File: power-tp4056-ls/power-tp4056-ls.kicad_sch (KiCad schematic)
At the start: 21 parts, among them J0 USB_C_Receptacle_PowerOnly_6P, J1 Conn_01x01, J2 Conn_01x01, J3 Conn_01x01, J4 Conn_01x01, J5 Conn_01x01, J6 Conn_01x01, Q1 AO3401A, U1 TP4056, U2 XB5307H

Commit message: Add LCSC part numbers for basic components
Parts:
- C1, C2: LCSC (none) -> C15850
- C3: LCSC (none) -> C28233
- D3: LCSC (none) -> C8678
- Q1: LCSC (none) -> C15127
- R1: LCSC (none) -> C17379
- R2: LCSC (none) -> C17408
- RN1: JLCPCB_CORRECTION (none) -> 0; 0; 90; LCSC (none) -> C29718
- U1: LCSC (none) -> C16581; LCSC Part C16581 -> (none)
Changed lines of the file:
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@@
 			)
 		)
+		(property "LCSC" "C29718"
+			(at 114.3 46.99 0)
+			(effects
+				(font
+					(size 1.27 1.27)
+				)
+				(hide yes)
+			)
+		)
+		(property "JLCPCB_CORRECTION" "0; 0; 90"
+			(at 114.3 46.99 90)
+			(effects
+				(font
+					(size 1.27 1.27)
+				)
+				(hide yes)
+			)
+		)
 		(pin "7"
 		)
@@
 			)
 		)
+		(property "LCSC" "C8678"
+			(at 236.22 35.56 0)
+			(effects
+				(font
+					(size 1.27 1.27)
+				)
+				(hide yes)
+			)
+		)
 		(pin "1"
 		)
@@
 			)
 		)
+		(property "LCSC" "C28233"
+			(at 252.73 71.12 0)
+			(effects
+				(font
+					(size 1.27 1.27)
+				)
+				(hide yes)
+			)
+		)
 		(pin "1"
 		)
@@
 			)
 		)
+		(property "LCSC" "C29718"
+			(at 247.65 41.91 0)
+			(effects
+				(font
+					(size 1.27 1.27)
+				)
+				(hide yes)
+			)
+		)
+		(property "JLCPCB_CORRECTION" "0; 0; 90"
+			(at 247.65 41.91 90)
+			(effects
+				(font
+					(size 1.27 1.27)
+				)
+				(hide yes)
+			)
+		)
 		(pin "7"
 		)
@@
 			)
 		)
+		(property "LCSC" "C15127"
+			(at 228.6 31.75 0)
+			(effects
+				(font
+					(size 1.27 1.27)
+				)
+				(hide yes)
+			)
+		)
 		(pin "1"
 		)
@@
 			)
 		)
+		(property "LCSC" "C17379"
+			(at 162.56 63.5 0)
+			(effects
+				(font
+					(size 1.27 1.27)
+				)
+				(hide yes)
+			)
+		)
 		(pin "1"
 		)
@@
 			)
 		)
+		(property "LCSC" "C15850"
+			(at 99.06 40.64 0)
+			(effects
+				(font
+					(size 1.27 1.27)
+				)
+				(hide yes)
+			)
+		)
 		(pin "1"
 		)
@@
 			)
 		)
+		(property "LCSC" "C17408"
+			(at 260.35 66.04 0)
+			(effects
+				(font
+					(size 1.27 1.27)
+				)
+				(hide yes)
+			)
+		)
 		(pin "2"
 		)
@@
 			)
 		)
-		(property "LCSC Part" "C16581"
-			(at 146.05 80.01 0)
+		(property "LCSC" "C16581"
+			(at 146.05 46.99 0)
 			(effects
 				(font
@@
 			)
 		)
+		(property "LCSC" "C29718"
+			(at 114.3 76.2 0)
+			(effects
+				(font
+					(size 1.27 1.27)
+				)
+				(hide yes)
+			)
+		)
+		(property "JLCPCB_CORRECTION" "0; 0; 90"
+			(at 114.3 76.2 90)
+			(effects
+				(font
+					(size 1.27 1.27)
+				)
+				(hide yes)
+			)
+		)
 		(pin "7"
 		)
@@
 			)
 		)
+		(property "LCSC" "C15850"
+			(at 179.07 36.83 0)
+			(effects
+				(font
+					(size 1.27 1.27)
+				)
+				(hide yes)
+			)
+		)
 		(pin "1"
 		)
@@
 			(effects
 				(font
+					(size 1.27 1.27)
+				)
+				(hide yes)
+			)
+		)
+		(property "LCSC" "C29718"
+			(at 114.3 59.69 0)
+			(effects
+				(font
+					(size 1.27 1.27)
+				)
+				(hide yes)
+			)
+		)
+		(property "JLCPCB_CORRECTION" "0; 0; 90"
+			(at 114.3 59.69 90)
+			(effects
+				(font

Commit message: Update LCSC part numbers and JLCPCB positioning info
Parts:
- C1, C2: LCSC C15850 -> (none); LCSC Part (none) -> C15850
- C3: LCSC C28233 -> (none); LCSC Part (none) -> C28233
- D3: LCSC C8678 -> (none); LCSC Part (none) -> C8678
- Q1: JLCPCB_CORRECTION (none) -> 0; 0; 180; LCSC C15127 -> (none); LCSC Part (none) -> C15127
- R1: LCSC C17379 -> (none); LCSC Part (none) -> C17379
- R2: LCSC C17408 -> (none); LCSC Part (none) -> C17408
- RN1: LCSC C29718 -> (none); LCSC Part (none) -> C29718
- U1: JLCPCB_CORRECTION (none) -> 0; 0; 270; LCSC C16581 -> (none); LCSC Part (none) -> C16581
- U2: JLCPCB_CORRECTION (none) -> 0; 0; 270
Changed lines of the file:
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@@
 			)
 		)
-		(property "LCSC" "C29718"
+		(property "LCSC Part" "C29718"
 			(at 114.3 46.99 0)
 			(effects
@@
 			)
 		)
-		(property "LCSC" "C8678"
+		(property "LCSC Part" "C8678"
 			(at 236.22 35.56 0)
 			(effects
@@
 			)
 		)
-		(property "LCSC" "C28233"
+		(property "LCSC Part" "C28233"
 			(at 252.73 71.12 0)
 			(effects
@@
 			)
 		)
-		(property "LCSC" "C29718"
+		(property "LCSC Part" "C29718"
 			(at 247.65 41.91 0)
 			(effects
@@
 			)
 		)
+		(property "JLCPCB_CORRECTION" "0; 0; 270"
+			(at 217.17 69.85 0)
+			(effects
+				(font
+					(size 1.27 1.27)
+				)
+				(hide yes)
+			)
+		)
 		(property "LCSC Part" "C154942"
 			(at 217.17 85.09 0)
@@
 			)
 		)
-		(property "LCSC" "C15127"
+		(property "LCSC Part" "C15127"
 			(at 228.6 31.75 0)
 			(effects
@@
 			)
 		)
+		(property "JLCPCB_CORRECTION" "0; 0; 180"
+			(at 228.6 31.75 90)
+			(effects
+				(font
+					(size 1.27 1.27)
+				)
+				(hide yes)
+			)
+		)
 		(pin "1"
 		)
@@
 			)
 		)
-		(property "LCSC" "C17379"
+		(property "LCSC Part" "C17379"
 			(at 162.56 63.5 0)
 			(effects
@@
 			)
 		)
-		(property "LCSC" "C15850"
+		(property "LCSC Part" "C15850"
 			(at 99.06 40.64 0)
 			(effects
@@
 			)
 		)
-		(property "LCSC" "C17408"
+		(property "LCSC Part" "C17408"
 			(at 260.35 66.04 0)
 			(effects
@@
 			)
 		)
-		(property "LCSC" "C16581"
+		(property "JLCPCB_CORRECTION" "0; 0; 270"
 			(at 146.05 46.99 0)
 			(effects
@@
 			)
 		)
+		(property "LCSC Part" "C16581"
+			(at 146.05 80.01 0)
+			(effects
+				(font
+					(size 1.27 1.27)
+				)
+				(hide yes)
+			)
+		)
 		(pin "9"
 		)
@@
 			)
 		)
-		(property "LCSC" "C29718"
+		(property "LCSC Part" "C29718"
 			(at 114.3 76.2 0)
 			(effects
@@
 			)
 		)
-		(property "LCSC" "C15850"
+		(property "LCSC Part" "C15850"
 			(at 179.07 36.83 0)
 			(effects
@@
 			)
 		)
-		(property "LCSC" "C29718"
+		(property "LCSC Part" "C29718"
 			(at 114.3 59.69 0)
 			(effects

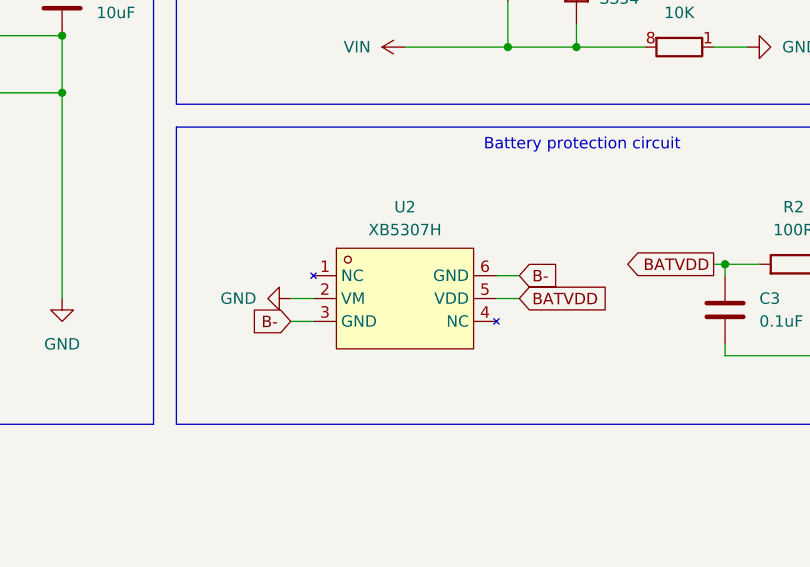
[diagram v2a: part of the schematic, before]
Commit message: Replace XB5307H with XB5350D0 for Li-Ion battery protection
XB5307H has an overcharge cutoff voltage of 4.425V, while XB5350D0 has
an overcharge cutoff voltage of 4.25V. Both ICs have an underdischarge
cutoff voltage of 3V.
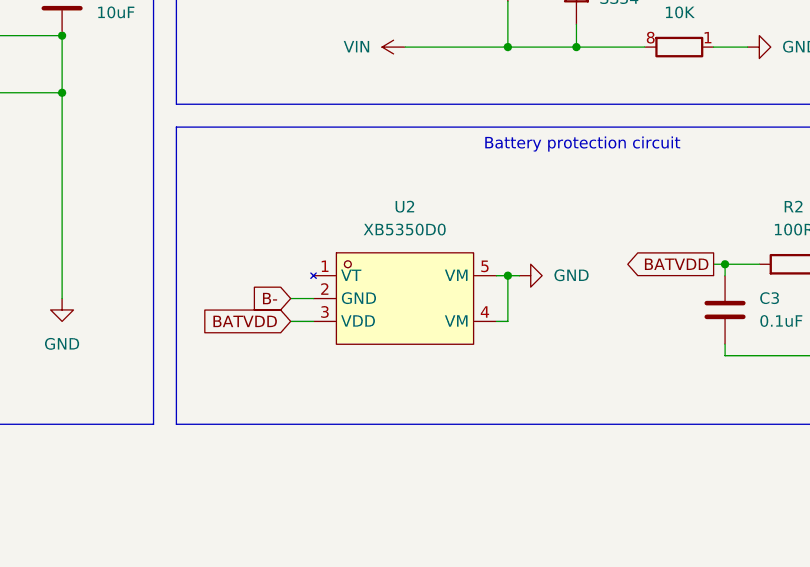
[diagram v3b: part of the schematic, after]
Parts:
- U2: value XB5307H -> XB5350D0; footprint Package_TO_SOT_SMD:SOT-23-6_Handsoldering -> custom:SOT-23-5_simple; symbol lcsc:XB5307H -> lcsc:XB5350D0; LCSC Part C154942 -> C2760002
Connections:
- net B-: now also U2.2 (GND); no longer U2.3 (GND), U2.6 (GND)
- net BATVDD: now also U2.3 (VDD); no longer U2.5 (VDD)
- net GND: now also U2.4 (VM), U2.5 (VM); no longer U2.2 (VM)
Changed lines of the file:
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@@
 	)
 	(junction
+		(at 228.6 67.31)
+		(diameter 0)
+		(color 0 0 0 0)
+	)
+	(junction
 		(at 54.61 59.69)
 		(diameter 0)
@@
 	(wire
 		(pts
-			(xy 229.87 67.31) (xy 227.33 67.31)
+			(xy 229.87 67.31) (xy 228.6 67.31)
 		)
 		(stroke
@@
 	(wire
 		(pts
-			(xy 229.87 69.85) (xy 227.33 69.85)
-		)
-		(stroke
-			(width 0)
-			(type default)
-		)
-	)
-	(wire
-		(pts
 			(xy 52.07 31.75) (xy 64.77 31.75)
 		)
@@
 	(wire
 		(pts
+			(xy 228.6 67.31) (xy 227.33 67.31)
+		)
+		(stroke
+			(width 0)
+			(type default)
+		)
+	)
+	(wire
+		(pts
 			(xy 64.77 54.61) (xy 64.77 59.69)
 		)
@@
 	(wire
 		(pts
+			(xy 228.6 72.39) (xy 228.6 67.31)
+		)
+		(stroke
+			(width 0)
+			(type default)
+		)
+	)
+	(wire
+		(pts
 			(xy 54.61 54.61) (xy 54.61 59.69)
 		)
@@
 	(wire
 		(pts
+			(xy 227.33 72.39) (xy 228.6 72.39)
+		)
+		(stroke
+			(width 0)
+			(type default)
+		)
+	)
+	(wire
+		(pts
 			(xy 252.73 66.04) (xy 252.73 67.31)
 		)
@@
 		)
 	)
+	(global_label "B-"
+		(shape input)
+		(at 204.47 69.85 180)
+		(fields_autoplaced yes)
+		(effects
+			(font
+				(size 1.27 1.27)
+			)
+			(justify right)
+		)
+		(property "Intersheetrefs" "${INTERSHEET_REFS}"
+			(at 198.6424 69.85 0)
+			(effects
+				(font
+					(size 1.27 1.27)
+				)
+				(justify right)
+				(hide yes)
+			)
+		)
+	)
 	(global_label "B+"
 		(shape output)
@@
 		)
 	)
-	(global_label "B-"
+	(global_label "BATVDD"
 		(shape input)
-		(at 229.87 67.31 0)
+		(at 204.47 72.39 180)
 		(fields_autoplaced yes)
 		(effects
@@
 				(size 1.27 1.27)
 			)
-			(justify left)
+			(justify right)
 		)
 		(property "Intersheetrefs" "${INTERSHEET_REFS}"
-			(at 235.6976 67.31 0)
+			(at 194.53 72.39 0)
 			(effects
 				(font
 					(size 1.27 1.27)
 				)
-				(justify left)
+				(justify right)
 				(hide yes)
 			)
@@
 		)
 	)
-	(global_label "B-"
-		(shape input)
-		(at 204.47 72.39 180)
-		(fields_autoplaced yes)
-		(effects
-			(font
-				(size 1.27 1.27)
-			)
-			(justify right)
-		)
-		(property "Intersheetrefs" "${INTERSHEET_REFS}"
-			(at 198.6424 72.39 0)
-			(effects
-				(font
-					(size 1.27 1.27)
-				)
-				(justify right)
-				(hide yes)
-			)
-		)
-	)
 	(global_label "BATVDD"
 		(shape output)
@@
 		)
 	)
-	(global_label "BATVDD"
-		(shape input)
-		(at 229.87 69.85 0)
-		(fields_autoplaced yes)
-		(effects
-			(font
-				(size 1.27 1.27)
-			)
-			(justify left)
-		)
-		(property "Intersheetrefs" "${INTERSHEET_REFS}"
-			(at 239.81 69.85 0)
-			(effects
-				(font
-					(size 1.27 1.27)
-				)
-				(justify left)
-				(hide yes)
-			)
-		)
-	)
 	(symbol
 		(lib_name "Conn_01x01_1")
@@
 	)
 	(symbol
-		(lib_id "lcsc:XB5307H")
+		(lib_id "lcsc:XB5350D0")
 		(at 217.17 69.85 0)
 		(unit 1)
@@
 			)
 		)
-		(property "Value" "XB5307H"
+		(property "Value" "XB5350D0"
 			(at 217.17 62.23 0)
 			(effects
@@
 			)
 		)
-		(property "Footprint" "Package_TO_SOT_SMD:SOT-23-6_Handsoldering"
+		(property "Footprint" "custom:SOT-23-5_simple"
 			(at 217.17 80.01 0)
 			(effects
@@
 		)
 		(property "Datasheet" "https://lcsc.com/product-detail/Battery-Protection-ICs_XB5307H_C154942.html"
-			(at 217.17 82.55 0)
+			(at 217.17 69.85 0)
 			(effects
 				(font
@@
 			)
 		)
-		(property "LCSC Part" "C154942"
-			(at 217.17 85.09 0)
+		(property "LCSC Part" "C2760002"
+			(at 217.17 82.55 0)
 			(effects
 				(font
@@
 		(pin "2"
 		)
-		(pin "6"
-		)
 		(pin "1"
 		)
@@
 	)
 	(symbol
+		(lib_id "power:GND")
+		(at 229.87 67.31 90)
+		(unit 1)
+		(exclude_from_sim no)
+		(in_bom yes)
+		(on_board yes)
+		(dnp no)
+		(fields_autoplaced yes)
+		(property "Reference" "#PWR04"
+			(at 236.22 67.31 0)
+			(effects
+				(font
+					(size 1.27 1.27)
+				)
+				(hide yes)
+			)
+		)
+		(property "Value" "GND"
+			(at 233.68 67.3099 90)
+			(effects
+				(font
+					(size 1.27 1.27)
+				)
+				(justify right)
+			)
+		)
+		(property "Footprint" ""
+			(at 229.87 67.31 0)
+			(effects
+				(font
+					(size 1.27 1.27)
+				)
+				(hide yes)
+			)
+		)
+		(property "Datasheet" ""
+			(at 229.87 67.31 0)
+			(effects
+				(font
+					(size 1.27 1.27)
+				)
+				(hide yes)
+			)
+		)
+		(property "Description" "Power symbol creates a global label with name \"GND\" , ground"
+			(at 229.87 67.31 0)
+			(effects
+				(font
+					(size 1.27 1.27)
+				)
+				(hide yes)
+			)
+		)
+		(pin "1"
+		)
+		(instances
+			(project "power-tp4056-ls"
+				(path "/f7334e40-25a3-4306-9a4a-47752c843a90"
+					(reference "#PWR04")
+					(unit 1)
+				)
+			)
+		)
+	)
+	(symbol
 		(lib_id "Connector_Generic:Conn_01x01")
 		(at 109.22 175.26 0)
@@
 				)
 			)
-		)
-	)
-	(symbol
-		(lib_id "power:GND")
-		(at 204.47 69.85 270)
-		(unit 1)
-		(exclude_from_sim no)
-		(in_bom yes)
-		(on_board yes)
-		(dnp no)
-		(fields_autoplaced yes)
-		(property "Reference" "#PWR021"
-			(at 198.12 69.85 0)
-			(effects
-				(font
-					(size 1.27 1.27)
-				)
-				(hide yes)
-			)
-		)
-		(property "Value" "GND"
-			(at 200.66 69.8499 90)
-			(effects
-				(font
-					(size 1.27 1.27)
-				)
-				(justify right)
-			)
-		)
-		(property "Footprint" ""
-			(at 204.47 69.85 0)
-			(effects
-				(font
-					(size 1.27 1.27)
-				)
-				(hide yes)
-			)
-		)
-		(property "Datasheet" ""
-			(at 204.47 69.85 0)
-			(effects
-				(font
-					(size 1.27 1.27)
-				)
-				(hide yes)
-			)
-		)
-		(property "Description" "Power symbol creates a global label with name \"GND\" , ground"
-			(at 204.47 69.85 0)
-			(effects
-				(font
-					(size 1.27 1.27)
-				)
-				(hide yes)
-			)
-		)
-		(pin "1"
-		)
-		(instances
-			(project "power-tp4056-ls"
-				(path "/f7334e40-25a3-4306-9a4a-47752c843a90"
-					(reference "#PWR021")
-					(unit 1)
-				)
-			)
